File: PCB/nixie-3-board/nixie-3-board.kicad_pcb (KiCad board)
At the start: 2 copper layers, 13 parts, among them Q1 MPSA42, Q2 MPSA92, U1 74141, U2 74141, U3 74HC595

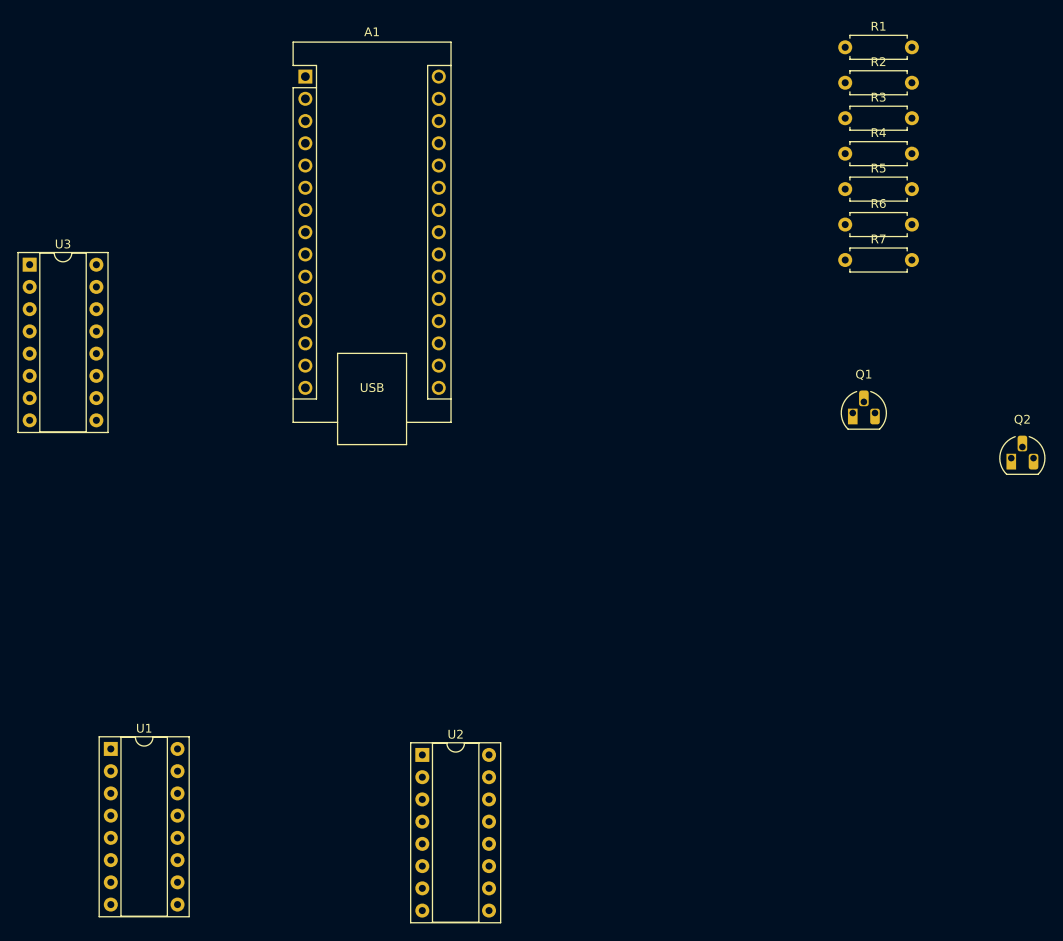
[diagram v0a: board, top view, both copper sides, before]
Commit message: Added more stuff for PCB abd added docs
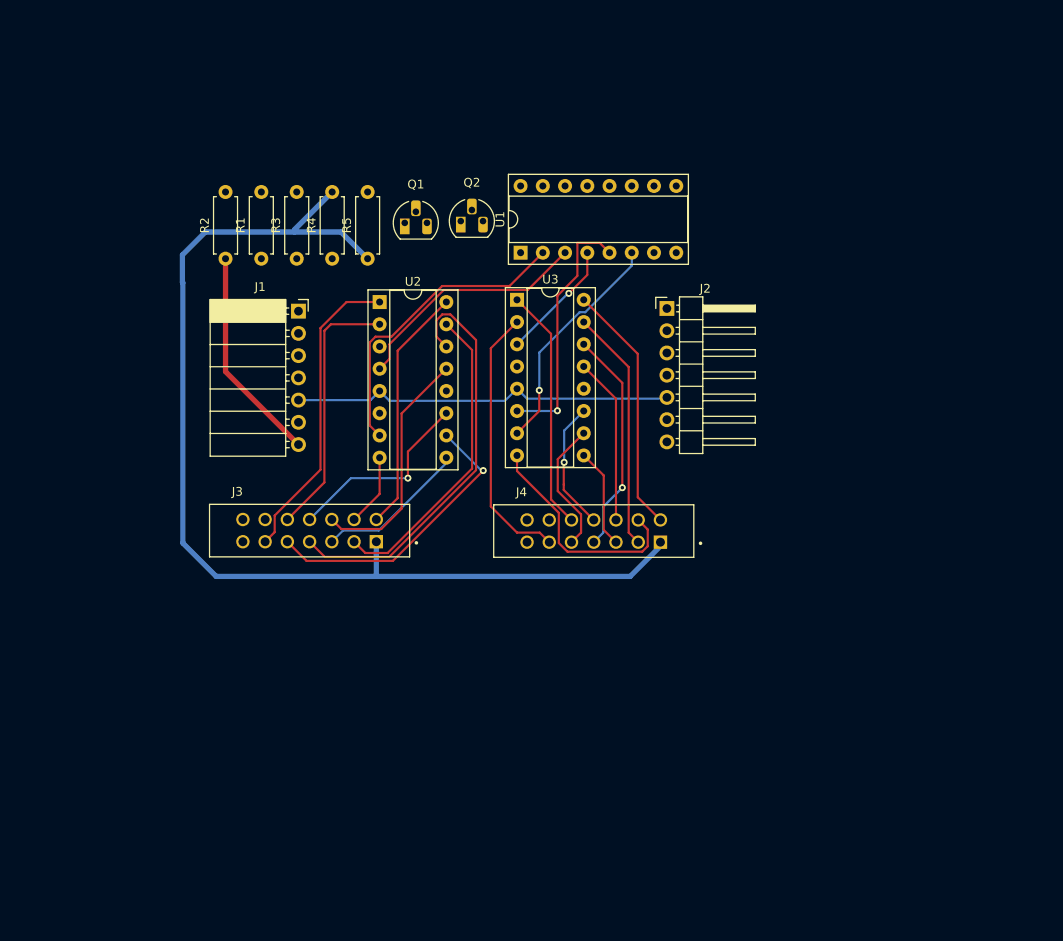
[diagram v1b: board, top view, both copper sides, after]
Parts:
- removed A1: Arduino_Nano_v3.x, Module:Arduino_Nano
- removed R6: 15K, Resistor_THT:R_Axial_DIN0207_L6.3mm_D2.5mm_P7.62mm_Horizontal
- removed R7: 220K, Resistor_THT:R_Axial_DIN0207_L6.3mm_D2.5mm_P7.62mm_Horizontal
- added J1: Conn_01x07_Socket, Connector_PinSocket_2.54mm:PinSocket_1x07_P2.54mm_Horizontal, F.Cu at (71.0, 62.1)
- added J2: Conn_01x07_Pin, Connector_PinHeader_2.54mm:PinHeader_1x07_P2.54mm_Horizontal, F.Cu at (113.1, 61.8)
- added J3: SFH11-PBPC-D07-ST-BK, nixie-3-footprints:SULLINS_SFH11-PBPC-D07-ST-BK, F.Cu at (72.3, 87.2)
- added J4: SFH11-PBPC-D07-ST-BK, nixie-3-footprints:SULLINS_SFH11-PBPC-D07-ST-BK, F.Cu at (104.7, 87.2)
- R1: value 15K -> 10K
- R2: value 220K -> 10K
- R3: value 10K -> 1M
- R4: value 10K -> 7.5K
- R5: value 1M -> 220K
- U1: value 74141 -> 74HC595
- U3: value 74HC595 -> 74141
- moved R2 73.6 mm to (62.7, 56.1), turned to 90 degrees
- moved U1 73.5 mm to (96.4, 55.4), turned to 90 degrees
- moved R1 70.9 mm to (66.8, 56.1), turned to 90 degrees
- moved Q2 68.5 mm to (89.6, 51.8)
- moved R3 64.7 mm to (70.8, 56.1), turned to 90 degrees
- moved R4 59.8 mm to (74.9, 56.1), turned to 90 degrees
- moved U3 55.8 mm to (96.0, 60.8)
- moved Q1 55.6 mm to (83.2, 52.0)
- moved R5 55.1 mm to (78.9, 56.1), turned to 90 degrees
- moved U2 52.0 mm to (80.3, 61.1)
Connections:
- R1 pad 1: Net-(Q2-C) -> HV_CNTRL
- R1 pad 2: T2 -> Net-(Q1-B)
- R2 pad 1: T2 -> HV
- R2 pad 2: GND -> Net-(Q2-B)
- R3 pad 1: HV_CNTRL -> Net-(Q2-B)
- R3 pad 2: Net-(Q1-B) -> Net-(Q1-C)
- R4 pad 1: HV -> Net-(Q2-C)
- R4 pad 2: Net-(Q2-B) -> /T
- R5 pad 1: Net-(Q2-B) -> /T
- R5 pad 2: Net-(Q1-C) -> GND
- U1 pad 1: unconnected-(U1-~{Q8}-Pad1) -> /LSD B
- U1 pad 10: unconnected-(U1-~{Q7}-Pad10) -> VCC
- U1 pad 11: unconnected-(U1-~{Q6}-Pad11) -> SRCLK
- U1 pad 12: GND -> RCLK
- U1 pad 13: unconnected-(U1-~{Q4}-Pad13) -> GND
- U1 pad 14: unconnected-(U1-~{Q5}-Pad14) -> SER
- U1 pad 15: unconnected-(U1-~{Q1}-Pad15) -> /LSD A
- U1 pad 16: unconnected-(U1-~{Q0}-Pad16) -> VCC
- U1 pad 2: unconnected-(U1-~{Q9}-Pad2) -> /LSD C
- U1 pad 3: /LSD A -> /LSD D
- U1 pad 4: /LSD D -> /MSD A
- U1 pad 5: VCC -> /MSD B
- U1 pad 6: /LSD B -> /MSD C
- U1 pad 7: /LSD C -> /MSD D
- U1 pad 8: unconnected-(U1-~{Q2}-Pad8) -> GND
- U1 pad 9: unconnected-(U1-~{Q3}-Pad9) -> SER_OUT
- U2 pad 1: unconnected-(U2-~{Q8}-Pad1) -> /D1-8
- U2 pad 10: unconnected-(U2-~{Q7}-Pad10) -> /D1-7
- U2 pad 11: unconnected-(U2-~{Q6}-Pad11) -> /D1-6
- U2 pad 13: unconnected-(U2-~{Q4}-Pad13) -> /D1-4
- U2 pad 14: unconnected-(U2-~{Q5}-Pad14) -> /D1-5
- U2 pad 15: unconnected-(U2-~{Q1}-Pad15) -> /D1-1
- U2 pad 16: unconnected-(U2-~{Q0}-Pad16) -> /D1-0
- U2 pad 2: unconnected-(U2-~{Q9}-Pad2) -> /D1-9
- U2 pad 3: /MSD A -> /LSD A
- U2 pad 4: /MSD D -> /LSD D
- U2 pad 6: /MSD B -> /LSD B
- U2 pad 7: /MSD C -> /LSD C
- U2 pad 8: unconnected-(U2-~{Q2}-Pad8) -> /D1-2
- U2 pad 9: unconnected-(U2-~{Q3}-Pad9) -> /D1-3
- U3 pad 1: /LSD B -> /D2-8
- U3 pad 10: VCC -> /D2-7
- U3 pad 11: /SRCLK -> /D2-6
- U3 pad 12: /RCLK -> GND
- U3 pad 13: GND -> /D2-4
- U3 pad 14: /SER -> /D2-5
- U3 pad 15: /LSD A -> /D2-1
- U3 pad 16: VCC -> /D2-0
- U3 pad 2: /LSD C -> /D2-9
- U3 pad 3: /LSD D -> /MSD A
- U3 pad 4: /MSD A -> /MSD D
- U3 pad 5: /MSD B -> VCC
- U3 pad 6: /MSD C -> /MSD B
- U3 pad 7: /MSD D -> /MSD C
- U3 pad 8: GND -> /D2-2
- U3 pad 9: unconnected-(U3-QH'-Pad9) -> /D2-3
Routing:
- net /T: track 0.00 -> 124.8 mm
- net /D1-5: track 0.00 -> 48.2 mm
- net VCC: track 0.00 -> 44.1 mm
- net /D1-1: track 0.00 -> 35.7 mm
- net /LSD C: track 0.00 -> 35.1 mm
- net /D1-8: track 0.00 -> 35.0 mm
- net /D1-7: track 0.00 -> 33.4 mm, vias 0 -> 1
- net /D2-9: track 0.00 -> 30.7 mm
- net /D1-9: track 0.00 -> 29.9 mm
- net /MSD B: track 0.00 -> 28.9 mm, vias 0 -> 1
- net /D2-0: track 0.00 -> 28.8 mm
- net /D1-0: track 0.00 -> 28.2 mm
- net /D2-1: track 0.00 -> 27.7 mm
- net /D2-8: track 0.00 -> 27.7 mm
- net /LSD D: track 0.00 -> 27.7 mm
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
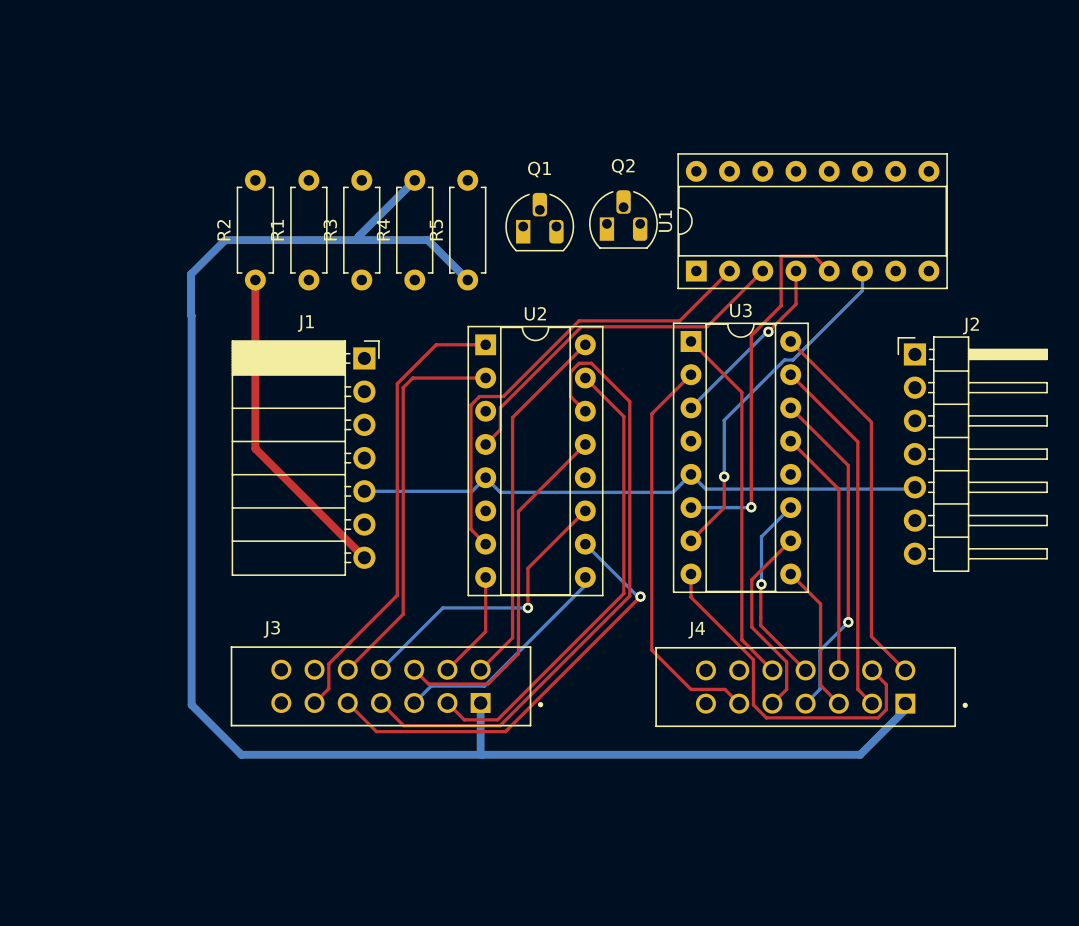
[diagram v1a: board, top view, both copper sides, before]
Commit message: new layout - might work. Needs holes, markings, screw terminals
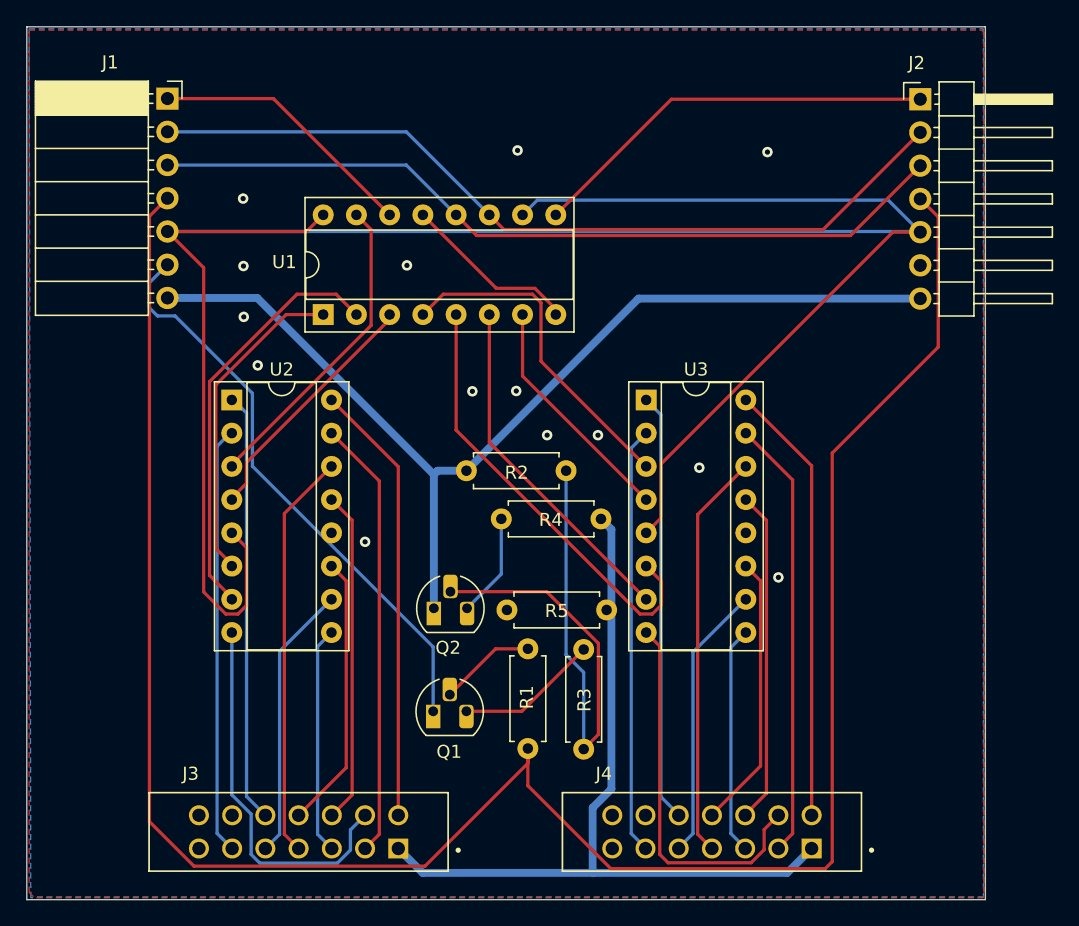
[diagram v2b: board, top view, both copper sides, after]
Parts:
- moved R3 39.7 mm to (87.8, 92.0)
- moved R1 39.5 mm to (83.5, 91.9)
- moved Q1 37.7 mm to (76.3, 89.1)
- moved Q2 32.2 mm to (76.3, 81.2)
- moved U1 28.7 mm to (67.9, 58.8)
- moved R5 27.4 mm to (89.5, 81.3), turned to 180 degrees
- moved J1 24.9 mm to (56.0, 42.2)
- moved R2 21.7 mm to (78.8, 70.7), turned to 0 degrees
- moved U2 19.9 mm to (60.9, 65.3)
- moved J2 19.5 mm to (113.5, 42.3)
- moved R4 19.4 mm to (81.5, 74.4), turned to 0 degrees
- moved J4 13.2 mm to (97.6, 98.3)
- moved J3 12.8 mm to (66.0, 98.3)
- moved U3 5.63 mm to (92.6, 65.3)
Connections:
- J3 pad 10: /D1-9 -> /D1-8
- J3 pad 11: /D1-8 -> /D1-9
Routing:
- net HV_CNTRL: track 0.00 -> 166.5 mm
- net VCC: track 44.1 -> 173.7 mm
- net SRCLK: track 0.00 -> 63.7 mm
- net /T: track 124.8 -> 61.5 mm
- net RCLK: track 0.00 -> 62.0 mm
- net GND: track 0.00 -> 58.0 mm, vias 0 -> 14
- net HV: track 24.7 -> 78.9 mm
- net Net-(Q2-B): track 0.00 -> 43.3 mm
- net SER_OUT: track 0.00 -> 31.5 mm
- net /LSD B: track 0.00 -> 24.7 mm
- net /LSD A: track 0.00 -> 24.0 mm
- net /D1-2: track 8.27 -> 29.0 mm
- net SER: track 0.00 -> 20.7 mm
- net /MSD D: track 0.00 -> 18.1 mm
- net /D1-5: track 48.2 -> 31.2 mm
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- added copper zone on B.Cu, net GND
- added copper zone on F.Cu, net GND
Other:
- board outline added: 73.3 x 66.7 mm

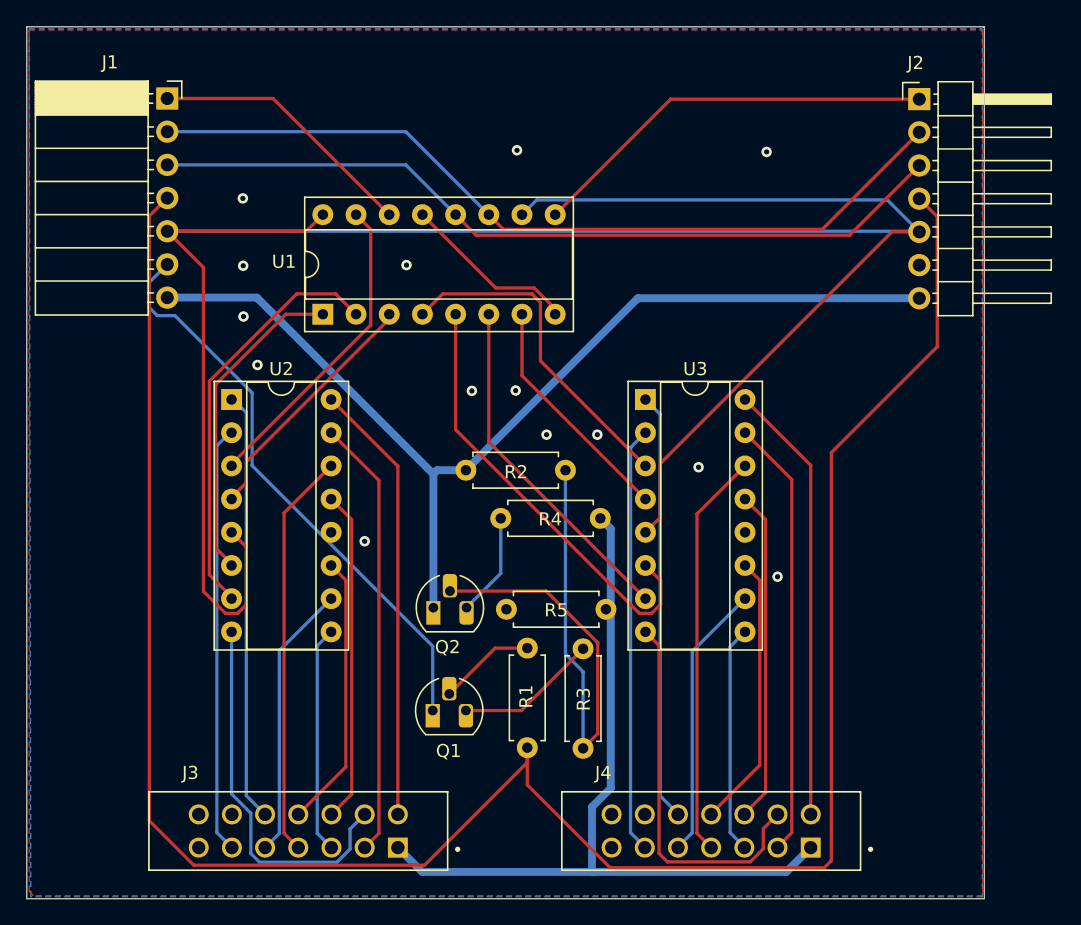
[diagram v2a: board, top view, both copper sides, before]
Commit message: Version 3 of the driver PCB
Adds decouping caps and re-orders digits so LSD is on the right.
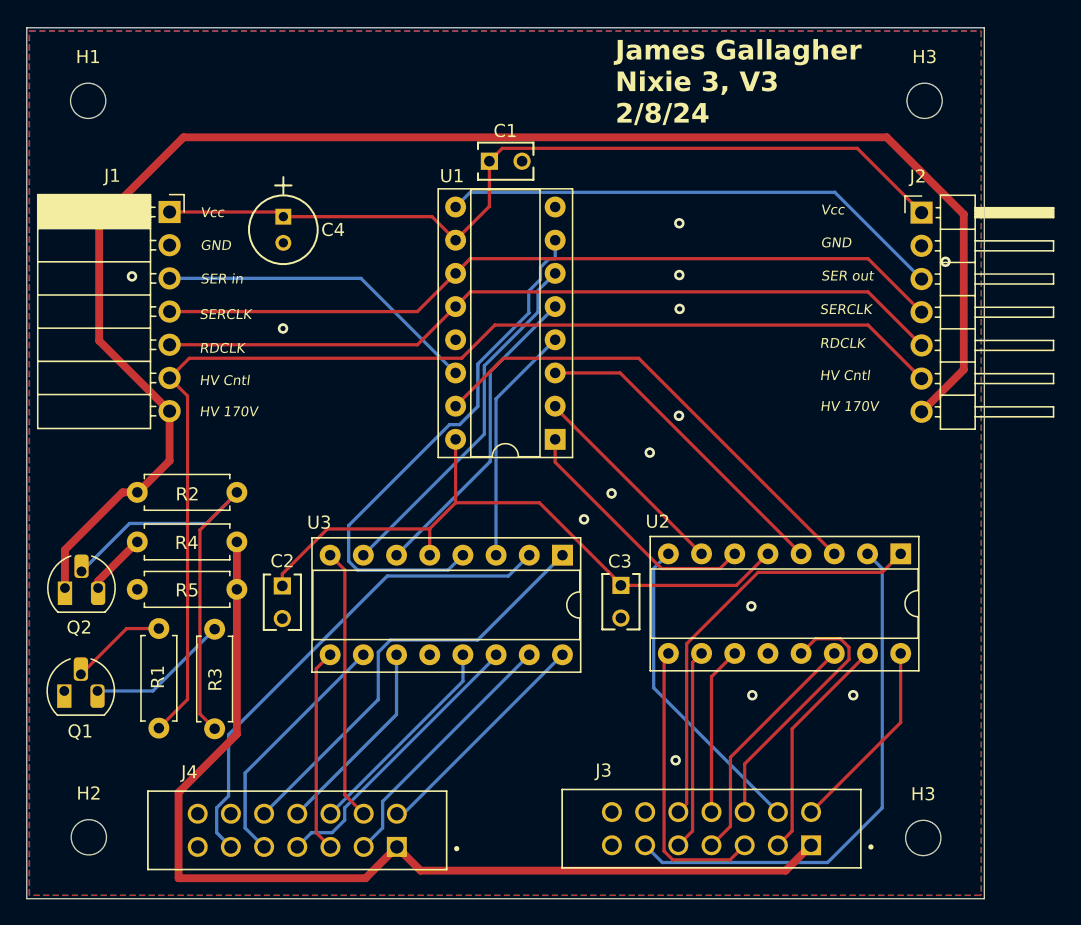
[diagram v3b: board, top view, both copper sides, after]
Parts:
- added C1: 100nF, nixie-3-footprints:K104Z15Y5VF5TL2_VIS, F.Cu at (80.6, 47.0)
- added C2: 100nF, nixie-3-footprints:K104Z15Y5VF5TL2_VIS, F.Cu at (64.8, 79.5)
- added C3: 100nF, nixie-3-footprints:K104Z15Y5VF5TL2_VIS, F.Cu at (90.7, 79.5)
- added C4: 100µF, nixie-3-footprints:U1-E_NCH, F.Cu at (64.8, 51.3)
- added H1: MountingHole, MountingHole:MountingHole_2.7mm_M2.5_DIN965, F.Cu at (49.9, 42.4)
- added H2: MountingHole, MountingHole:MountingHole_2.7mm_M2.5_DIN965, F.Cu at (50.0, 98.8)
- added H3: MountingHole, MountingHole:MountingHole_2.7mm_M2.5_DIN965, F.Cu at (113.9, 42.4)
- added H3: MountingHole, MountingHole:MountingHole_2.7mm_M2.5_DIN965, F.Cu at (113.8, 98.8)
- moved U2 52.6 mm to (112.1, 77.1), turned to -90 degrees
- moved J4 31.7 mm to (65.9, 98.2)
- moved J3 31.6 mm to (97.6, 98.1)
- moved R5 28.3 mm to (61.3, 79.8)
- moved Q1 28.2 mm to (48.1, 87.6)
- moved Q2 28.2 mm to (48.1, 79.7)
- moved R1 28.2 mm to (55.3, 90.4)
- moved R3 28.2 mm to (59.6, 90.5)
- moved R4 27.9 mm to (53.7, 76.2)
- moved R2 25.2 mm to (53.7, 72.4)
- moved U1 20.2 mm to (85.6, 68.3), turned to 180 degrees
- moved U3 13.5 mm to (86.2, 77.2), turned to -90 degrees
- moved J2 8.69 mm to (113.7, 51.0)
- moved J1 8.69 mm to (56.1, 50.9)
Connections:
- J1 pad 1: SER -> VCC
- J1 pad 2: SRCLK -> GND
- J1 pad 3: RCLK -> SER
- J1 pad 4: HV_CNTRL -> SRCLK
- J1 pad 5: VCC -> RCLK
- J1 pad 6: GND -> HV_CNTRL
- J2 pad 1: SER_OUT -> VCC
- J2 pad 2: SRCLK -> GND
- J2 pad 3: RCLK -> SER_OUT
- J2 pad 4: HV_CNTRL -> SRCLK
- J2 pad 5: VCC -> RCLK
- J2 pad 6: GND -> HV_CNTRL
- Q2 pad 3: Net-(Q2-C) -> HV
- R4 pad 1: Net-(Q2-C) -> HV
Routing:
- net HV_CNTRL: track 166.5 -> 89.2 mm
- net GND: track 58.0 -> 0.00 mm
- net VCC: track 173.7 -> 116.3 mm
- net HV: track 78.9 -> 126.7 mm
- net /MSD D: track 18.1 -> 41.4 mm
- net /D1-0: track 33.9 -> 15.0 mm
- net /T: track 61.5 -> 78.5 mm
- net /D1-1: track 33.7 -> 17.5 mm
- net /D2-0: track 33.8 -> 17.7 mm
- net /LSD C: track 31.9 -> 15.9 mm
- net /D2-1: track 33.6 -> 20.0 mm
- net /LSD A: track 24.0 -> 36.7 mm
- net /D1-5: track 31.2 -> 18.6 mm
- net /MSD B: track 34.1 -> 24.1 mm
- net /D2-5: track 31.2 -> 21.9 mm
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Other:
- board size 73.3 x 66.7 mm -> 73.3 x 66.6 mm
- board text added: "GND"
- board text added: "HV 170V"
- board text added: "HV Cntl"
- board text added: "James Gallagher Nixie 3, V3 2/8/24"
- board text added: "RDCLK"
- board text added: "SER in"
- board text added: "SER out"
- board text added: "SERCLK"
- board text added: "Vcc"

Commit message: Fixed mistakes, v3.1
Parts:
- removed the H3 at (113.9, 42.4)
- added H4: MountingHole, MountingHole:MountingHole_2.7mm_M2.5_DIN965, F.Cu at (113.9, 42.3)
- added REF**: OSHW-Logo2_14.6x12mm_SilkScreen, Symbol:OSHW-Logo2_14.6x12mm_SilkScreen, F.Cu at (96.8, 60.5)
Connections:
- Q2 pad 3: HV -> Net-(Q2-C)
- R4 pad 1: HV -> Net-(Q2-C)
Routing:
- net VCC: track 116.3 -> 139.3 mm, vias 0 -> 2
- net HV: track 126.7 -> 121.8 mm
- net Net-(Q2-C): track 0.00 -> 4.77 mm
- net /MSD C: track 27.6 -> 28.6 mm
- net /MSD D: track 41.4 -> 42.1 mm
- net GND: vias 14 -> 7
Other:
- board text added: "2/11/24"
- board text added: "James Gallagher Nixie 3, V3.1"
- board text removed: "James Gallagher Nixie 3, V3 2/8/24"

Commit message: Better names for the decoupling cap footprint files
Also corrected the value for the PS decoupling cap from 100uF to 10uF
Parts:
- removed REF**: OSHW-Logo2_14.6x12mm_SilkScreen, Symbol:OSHW-Logo2_14.6x12mm_SilkScreen
- C4: value 100µF -> 10µF
